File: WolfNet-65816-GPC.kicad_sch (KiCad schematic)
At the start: 1 part

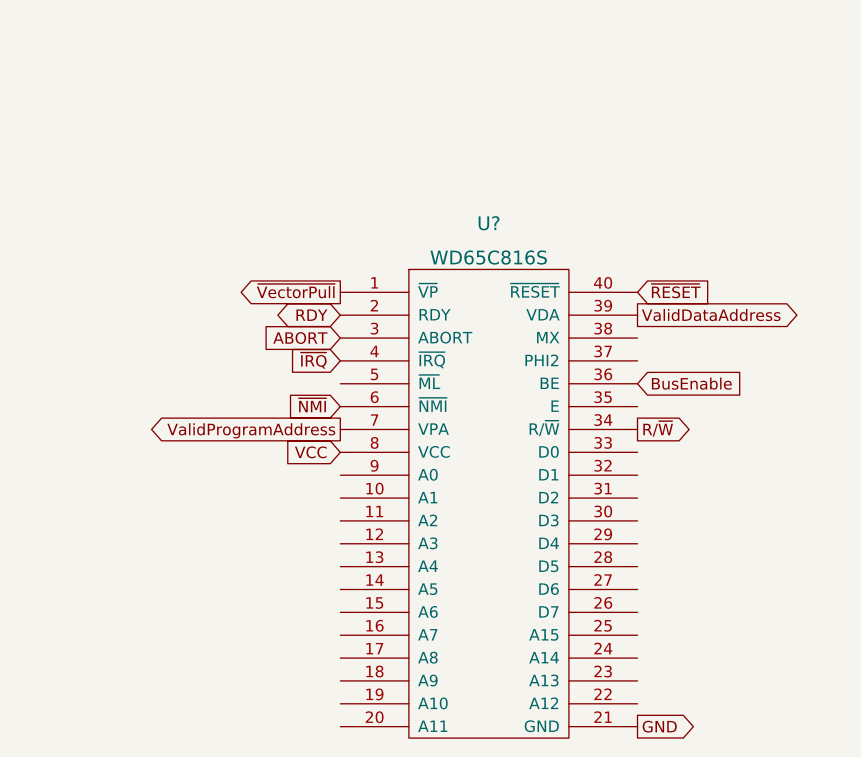
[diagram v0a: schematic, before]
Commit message: Added and connected CPU...
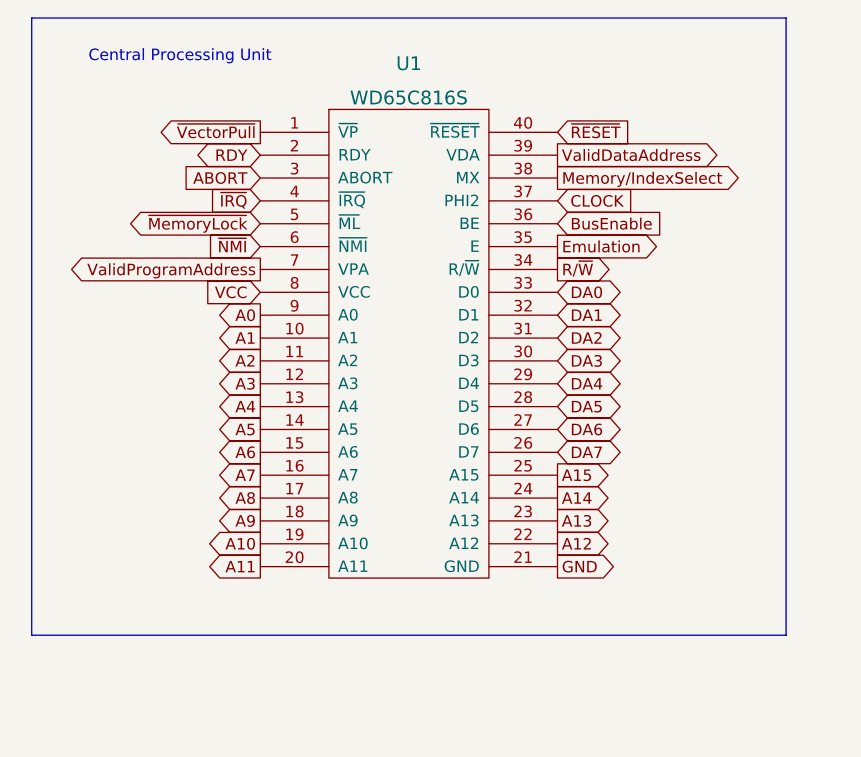
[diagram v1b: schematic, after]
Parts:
- gave numbers to parts that had none: 1
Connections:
- net A1: now reaches U1.10 (A1)
- net A2: now reaches U1.11 (A2)
- net A3: now reaches U1.12 (A3)
- net A4: now reaches U1.13 (A4)
- net A5: now reaches U1.14 (A5)
- net A6: now reaches U1.15 (A6)
- net A7: now reaches U1.16 (A7)
- net A8: now reaches U1.17 (A8)
- net A9: now reaches U1.18 (A9)
- net A10: now reaches U1.19 (A10)
- net A11: now reaches U1.20 (A11)
- net A12: now reaches U1.22 (A12)
- net A13: now reaches U1.23 (A13)
- net A14: now reaches U1.24 (A14)
- net A15: now reaches U1.25 (A15)
- net DA7: now reaches U1.26 (D7)
- net DA6: now reaches U1.27 (D6)
- net DA5: now reaches U1.28 (D5)
- net DA4: now reaches U1.29 (D4)
- net DA3: now reaches U1.30 (D3)
- net DA2: now reaches U1.31 (D2)
- net DA1: now reaches U1.32 (D1)
- net DA0: now reaches U1.33 (D0)
- net Emulation: now reaches U1.35 (E)
- net CLOCK: now reaches U1.37 (PHI2)
- net Memory/IndexSelect: now reaches U1.38 (MX)
- net ~{MemoryLock}: now reaches U1.5 (~{ML})
- net A0: now reaches U1.9 (A0)
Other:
- note added: "Central Processing Unit"
- moved on the sheet: U1

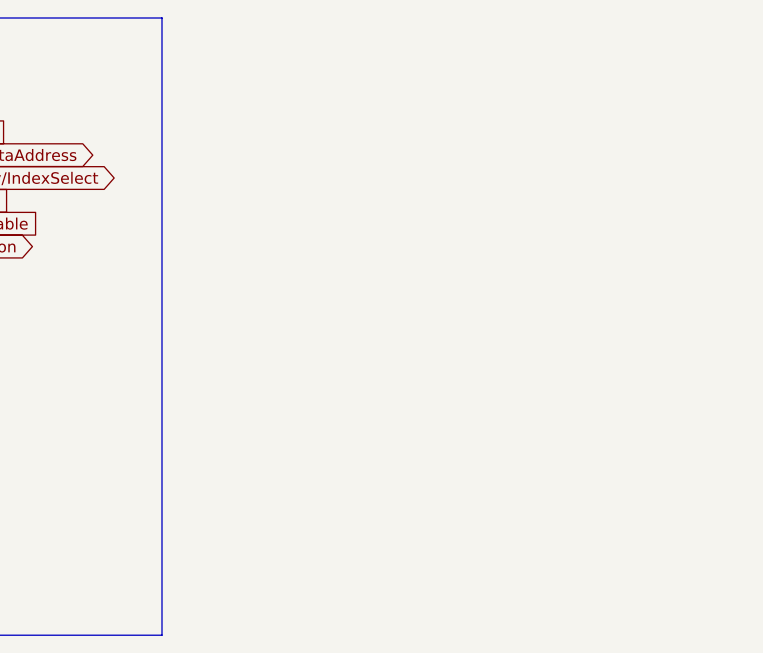
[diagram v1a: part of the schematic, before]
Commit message: Added and connected RAM...
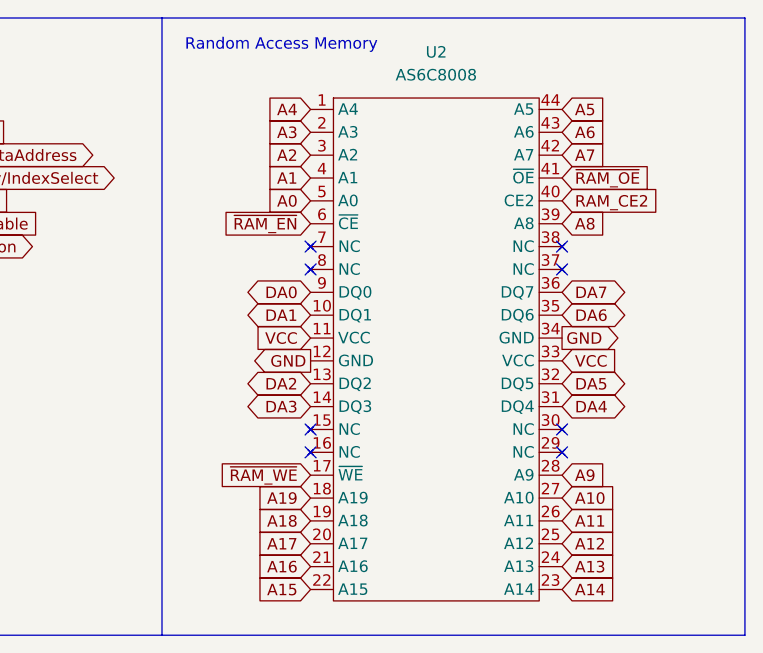
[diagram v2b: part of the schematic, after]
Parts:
- added U2: AS6C8008, symbol Memory:AS6C8008
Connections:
- net A0: now also U2.5 (A0)
- net A1: now also U2.4 (A1)
- net A10: now also U2.27 (A10)
- net A11: now also U2.26 (A11)
- net A12: now also U2.25 (A12)
- net A13: now also U2.24 (A13)
- net A14: now also U2.23 (A14)
- net A15: now also U2.22 (A15)
- net A2: now also U2.3 (A2)
- net A3: now also U2.2 (A3)
- net A4: now also U2.1 (A4)
- net A5: now also U2.44 (A5)
- net A6: now also U2.43 (A6)
- net A7: now also U2.42 (A7)
- net A8: now also U2.39 (A8)
- net A9: now also U2.28 (A9)
- net DA0: now also U2.9 (DQ0)
- net DA1: now also U2.10 (DQ1)
- net DA2: now also U2.13 (DQ2)
- net DA3: now also U2.14 (DQ3)
- net DA4: now also U2.31 (DQ4)
- net DA5: now also U2.32 (DQ5)
- net DA6: now also U2.35 (DQ6)
- net DA7: now also U2.36 (DQ7)
- net GND: now also U2.12 (GND), U2.34 (GND)
- net VCC: now also U2.11 (VCC), U2.33 (VCC)
- new net A16: U2.21 (A16)
- new net A17: U2.20 (A17)
- new net A18: U2.19 (A18)
- new net A19: U2.18 (A19)
- new net RAM_CE2: U2.40 (CE2)
- new net ~{RAM_EN}: U2.6 (~{CE})
- new net ~{RAM_OE}: U2.41 (~{OE})
- new net ~{RAM_WE}: U2.17 (~{WE})
- no-connect marks 0 -> 8
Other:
- note added: "Random Access Memory"

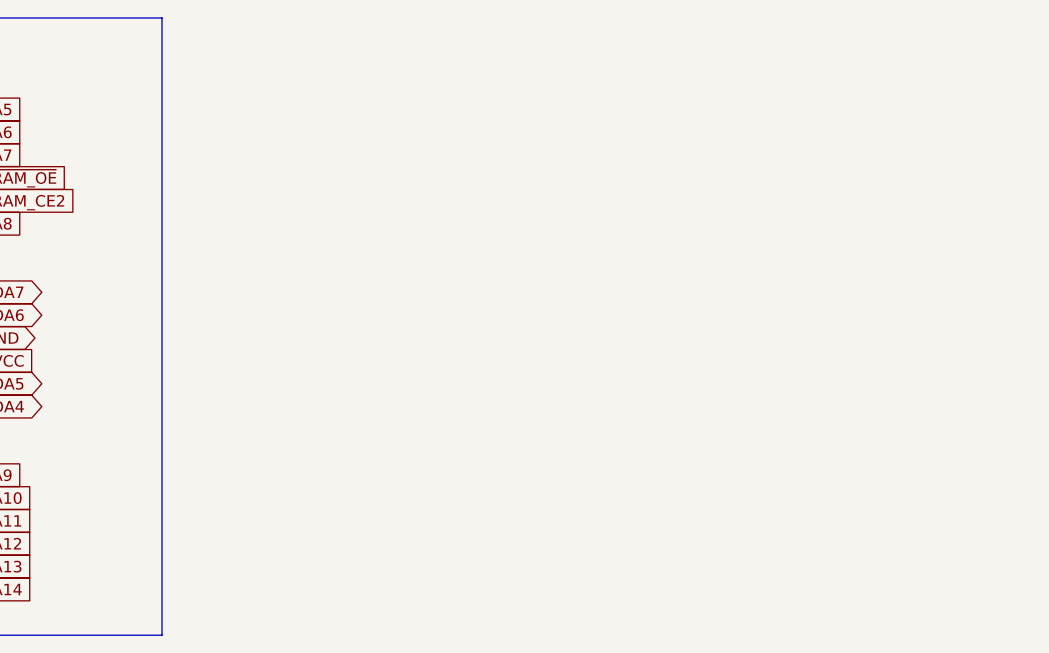
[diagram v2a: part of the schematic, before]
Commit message: Added and connected 2 ROM Banks...
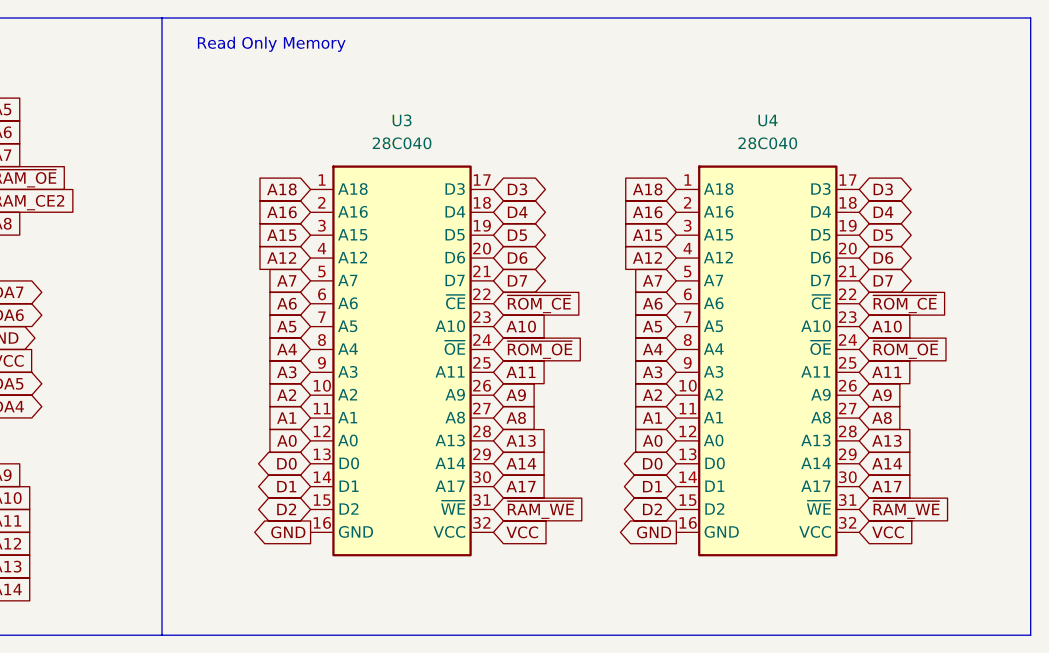
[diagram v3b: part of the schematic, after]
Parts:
- added U3, U4: 28C040, symbol Memory:28C040
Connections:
- net A0: now also U3.12 (A0), U4.12 (A0)
- net A1: now also U3.11 (A1), U4.11 (A1)
- net A10: now also U3.23 (A10), U4.23 (A10)
- net A11: now also U3.25 (A11), U4.25 (A11)
- net A12: now also U3.4 (A12), U4.4 (A12)
- net A13: now also U3.28 (A13), U4.28 (A13)
- net A14: now also U3.29 (A14), U4.29 (A14)
- net A15: now also U3.3 (A15), U4.3 (A15)
- net A16: now also U3.2 (A16), U4.2 (A16)
- net A17: now also U3.30 (A17), U4.30 (A17)
- net A18: now also U3.1 (A18), U4.1 (A18)
- net A2: now also U3.10 (A2), U4.10 (A2)
- net A3: now also U3.9 (A3), U4.9 (A3)
- net A4: now also U3.8 (A4), U4.8 (A4)
- net A5: now also U3.7 (A5), U4.7 (A5)
- net A6: now also U3.6 (A6), U4.6 (A6)
- net A7: now also U3.5 (A7), U4.5 (A7)
- net A8: now also U3.27 (A8), U4.27 (A8)
- net A9: now also U3.26 (A9), U4.26 (A9)
- net GND: now also U3.16 (GND), U4.16 (GND)
- net VCC: now also U3.32 (VCC), U4.32 (VCC)
- net ~{RAM_WE}: now also U3.31 (~{WE}), U4.31 (~{WE})
- new net D0: U3.13 (D0), U4.13 (D0)
- new net D1: U3.14 (D1), U4.14 (D1)
- new net D2: U3.15 (D2), U4.15 (D2)
- new net D3: U3.17 (D3), U4.17 (D3)
- new net D4: U3.18 (D4), U4.18 (D4)
- new net D5: U3.19 (D5), U4.19 (D5)
- new net D6: U3.20 (D6), U4.20 (D6)
- new net D7: U3.21 (D7), U4.21 (D7)
- new net ~{ROM_CE}: U3.22 (~{CE}), U4.22 (~{CE})
- new net ~{ROM_OE}: U3.24 (~{OE}), U4.24 (~{OE})
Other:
- note added: "Read Only Memory"

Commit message: Update WolfNet-65816-GPC.kicad_sch
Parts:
- removed U2: AS6C8008, symbol Memory:AS6C8008
- added SW1: SW_Push, symbol Switch:SW_Push
- added U5: 74HCT573, symbol 74xx:74LS573
- added U6: 74HCT245, symbol 74xx:74HC245
- added U7: 22V10, symbol GALs:22V10
- added U8: XCR3064XL-VQ100, Package_QFP:LQFP-100_14x14mm_P0.5mm, symbol CPLD_Xilinx:XCR3064XL-VQ100
- added U9: DS1813, symbol Supervisory Circuit:DS1813
- added U?: AS6C1608, symbol Memory:AS6C1608
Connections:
- net A0: now also U8.85 (A0), U?.5 (A0)
- net A1: now also U8.84 (A1), U?.4 (A1)
- net A10: now also U8.69 (A10), U?.27 (A10)
- net A11: now also U8.68 (A11), U?.26 (A11)
- net A12: now also U8.67 (A12), U?.25 (A12)
- net A13: now also U8.65 (A13), U?.24 (A13)
- net A14: now also U8.64 (A14), U?.23 (A14)
- net A15: now also U8.63 (A15), U?.22 (A15)
- net A16: now also U5.19 (Q0), U8.92 (B0), U?.21 (A16)
- net A17: now also U5.18 (Q1), U8.93 (B1), U?.20 (A17)
- net A18: now also U5.17 (Q2), U8.94 (B2), U?.19 (A18)
- net A19: now also U5.16 (Q3), U8.96 (B3), U?.18 (A19)
- net A2: now also U8.83 (A2), U?.3 (A2)
- net A3: now also U8.81 (A3), U?.2 (A3)
- net A4: now also U8.80 (A4), U?.1 (A4)
- net A5: now also U8.79 (A5), U?.44 (A5)
- net A6: now also U8.76 (A6), U?.43 (A6)
- net A7: now also U8.75 (A7), U?.42 (A7)
- net A8: now also U8.73 (A8/TDO), U?.39 (A8)
- net A9: now also U8.71 (A9), U?.28 (A9)
- net D0: now also U6.2 (A0), U?.9 (DQ0)
- net D1: now also U6.3 (A1), U?.10 (DQ1)
- net D2: now also U6.4 (A2), U?.13 (DQ2)
- net D3: now also U6.5 (A3), U?.14 (DQ3)
- net D4: now also U6.6 (A4), U?.31 (DQ4)
- net D5: now also U6.7 (A5), U?.32 (DQ5)
- net D6: now also U6.8 (A6), U?.35 (DQ6)
- net D7: now also U?.36 (DQ7)
- net DA0: now also U5.2 (D0), U6.18 (B0)
- net DA1: now also U5.3 (D1), U6.17 (B1)
- net DA2: now also U5.4 (D2), U6.16 (B2)
- net DA3: now also U5.5 (D3), U6.15 (B3)
- net DA4: now also U5.6 (D4), U6.14 (B4)
- net DA5: now also U5.7 (D5), U6.13 (B5)
- net DA6: now also U5.8 (D6), U6.12 (B6)
- net DA7: now also U5.9 (D7), U6.11 (B7)
- net GND: now also SW1.2, U5.1 (OE), U5.10 (GND), U6.10 (GND), U7.12 (GND), U8.26 (GND), U8.38 (GND), U8.43 (GND), U8.59 (GND), U8.74 (GND), U8.86 (GND), U8.95 (GND), U9.3 (GND), U?.12 (GND), U?.34 (GND)
- net RAM_CE2: now also U?.40 (CE2)
- net R/~{W}: now also U6.1 (A->B), U7.2 (IN)
- net ~{RAM_EN}: now also U?.6 (~{CE})
- net ~{RAM_OE}: now also U?.41 (~{OE})
- net ~{RAM_WE}: now also U?.17 (~{WE})
- net ~{RESET}: now also SW1.1, U9.1 (~{RST})
- net VCC renamed +5V
- net +5V: now also U5.20 (VCC), U6.20 (VCC), U7.24 (VCC), U8.18 (VCC), U8.3 (VCC), U8.34 (VCC), U8.39 (VCC), U8.51 (VCC), U8.66 (VCC), U8.82 (VCC), U8.91 (VCC), U9.2 (VCC), U?.11 (VCC), U?.33 (VCC)
- new net A20: U5.15 (Q4), U8.97 (B4), U?.16 (A20)
- new net A21: U5.14 (Q5), U8.98 (B5)
- new net A22: U5.13 (Q6), U8.99 (B6)
- new net A23: U5.12 (Q7), U8.100 (B7)
- new net D8: U6.9 (A7)
- new net DecoderJTAG: U8.11 (PORT_EN)
- new net NOT_PHI2: U5.11 (Load), U6.19 (CE), U7.23 (I/O)
- new net PHI2: U7.1 (CLK/IN), U8.90 (CLK0/IN0)
- new net READ: U7.22 (I/O)
- new net WRITE: U7.21 (I/O)
- no-connect marks 8 -> 7
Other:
- note added: "Address Decoding"
- note added: "Bank Address Latch"
- note added: "Direct Memory Access Circuit"
- note added: "Memory Management"
- note added: "Supervisory Circuit"

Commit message: Almost there...
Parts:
- added D?: PWR_OK1, symbol Device:LED
- added J1: ATX-24, symbol Connector:ATX-24
- added R?: 220 Ω, symbol Device:R
- added R?: PWR220T-20-5R00J, symbol Device:R
- added SW1: SW_SPST, symbol Switch:SW_SPST
- added U5: XCR3064XL-VQ100, Package_QFP:LQFP-100_14x14mm_P0.5mm, symbol CPLD_Xilinx:XCR3064XL-VQ100
- added U?: SC28L91, symbol UART:SC28L91
- added U?: MCP2200-I-SO, Package_SO:SOIC-20W_7.5x12.8mm_P1.27mm, symbol Interface_USB:MCP2200-I-SO
- gave numbers to parts that had none: 1
- renumbered SW1 to SW2, U9 to U10, U5 to U2, U6 to U3, U3 to U6, U4 to U7, U7 to U8, U8 to U9
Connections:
- net +5V: now also J1.21 (+5V), J1.22 (+5V), J1.23 (+5V), J1.4 (+5V), J1.6 (+5V), R?.1, U5.18 (VCC), U5.3 (VCC), U5.34 (VCC), U5.39 (VCC), U5.51 (VCC), U5.66 (VCC), U5.82 (VCC), U5.91 (VCC), U?.11 (VCC), U?.12 (MODE_SELECT), U?.44 (VCC)
- net A0: now also U?.2 (A0)
- net A1: now also U?.4 (A1)
- net A2: now also U?.6 (A2)
- net A3: now also U?.7 (A3)
- net GND: now also D?.1 (K), J1.15 (GND), J1.17 (GND), J1.18 (GND), J1.19 (GND), J1.24 (GND), J1.3 (GND), J1.5 (GND), J1.7 (GND), R?.2, SW1.1 (A), U5.26 (GND), U5.38 (GND), U5.43 (GND), U5.59 (GND), U5.74 (GND), U5.86 (GND), U5.95 (GND), U?.22 (GND)
- net PHI2: now also U5.90 (CLK0/IN0)
- net ~{RESET}: now also U?.4 (RST)
- net READ renamed ~{READ}
- net ~{READ}: now also U?.10 (~{RD})
- net WRITE renamed ~{WRITE}
- net ~{WRITE}: now also U?.9 (~{WR})
- new net: J1.8 (PWR_OK), R?.1
- new net: D?.2 (A), R?.2
- new net: J1.1 (+3.3V), J1.12 (+3.3V), J1.13 (+3.3V), J1.2 (+3.3V)
- new net: J1.16 (PS_ON#), SW1.2 (B)
- new net +12V: J1.10 (+12V), J1.11 (+12V)
- new net -12V: J1.14 (-12V)
- new net DMA_JTAG: U5.11 (PORT_EN)
- no-connect marks 7 -> 9
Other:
- note added: "ATX power connector"
- note added: "UART"
- note added: "USB Connection"

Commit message: Update WolfNet-65816-GPC.kicad_sch
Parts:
- removed U8: 22V10, symbol GALs:22V10
- added C?: 10 µF, symbol Device:C
- added D? (x2): GREEN, symbol Device:LED
- added J? (x4): Conn_01x01, symbol Connector_Generic:Conn_01x01
- added R? (x2): R, symbol Device:R
- added X?: ACO-12MHz, Oscillator:Oscillator_DIP-14, symbol Oscillator:ACO-xxxMHz
- added X?: ACO-xxxMHz, Oscillator:Oscillator_DIP-14, symbol Oscillator:ACO-xxxMHz
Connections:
- net +5V: now also X?.14 (Vcc), X?.14 (Vcc)
- net A8: now also J?.1 (Pin_1)
- net D0: now also U?.28 (D0)
- net D1: now also U?.18 (D1)
- net D2: now also U?.27 (D2)
- net D3: now also U?.19 (D3)
- net D4: now also U?.26 (D4)
- net D5: now also U?.20 (D5)
- net D6: now also U?.25 (D6)
- net D7: now also U?.21 (D7)
- net GND: now also U?.20 (VSS), C?.1, D?.1 (K), D?.1 (K), X?.7 (GND), X?.7 (GND)
- net NOT_PHI2: now also U9.4 (B8/TDI), J?.1 (Pin_1)
- net R/~{W}: now also U9.9 (B11); no longer U3.1 (A->B)
- net ~{IRQ}: now also U?.24 (~{IRQ})
- net ~{RAM_EN}: now also U9.37 (D15)
- net ~{READ}: now also U9.10 (B12)
- net ~{RESET}: now also U?.38 (RESET)
- net ~{WRITE}: now also U3.1 (A->B), U9.12 (B13)
- net at U9.15 (D0/TMS): now also J?.1 (Pin_1)
- net ~{UART_EN}: now reaches U9.29 (D8)
- net ~{UART_EN}: now also U?.39 (~{CE})
- net ~{ROM2_EN}: now reaches U9.31 (D10)
- net ~{ROM2_EN}: now also U7.22 (~{CE})
- net ~{ROM1_EN}: now reaches U9.33 (D12)
- net ~{ROM1_EN}: now also U6.22 (~{CE})
- net at U9.62 (C0/TCK): now also J?.1 (Pin_1)
- net TxD: now reaches U?.33 (TxD)
- net TxD: now also U?.12 (RX)
- net RxD: now reaches U?.35 (RxD)
- net RxD: now also U?.10 (TX)
- net at U?.36 (X1/CLK): now also X?.8 (OUT)
- net VBUS: now reaches U?.1 (VDD)
- net at U?.17 (V_USB): now also C?.2
- net USB_D-: now reaches U?.18 (D-)
- net USB_D+: now reaches U?.19 (D+)
- net at U?.2 (OSC1): now also X?.8 (OUT)
- net at U?.5 (GP7/TxLED): now also R?.1
- net at U?.6 (GP6/RxLED): now also R?.1
- net RAM_CE2 renamed RAM_EN2
- removed net ~{ROM_CE}: U6.22 (~{CE}), U7.22 (~{CE})
- net ~{ROM_OE} renamed ~{ROM1_OE}
- net ~{ROM1_OE}: no longer U7.24 (~{OE})
- new net: D?.2 (A), R?.2 (x2)
- new net ~{ROM2_OE}: U7.24 (~{OE})
- no-connect marks 9 -> 38
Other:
- note removed: "Memory Management"

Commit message: Update WolfNet-65816-GPC.kicad_sch
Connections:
- net RAM_EN2: now also U9.36 (D14)
- net ~{RAM_OE}: now also U9.35 (D13)
- net ~{ROM1_OE}: now also U9.32 (D11)
- net ~{ROM2_OE}: now also U9.30 (D9)
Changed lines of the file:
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@@
+    )
+  )
+  (global_label "RAM_EN2" (shape output) (at 336.55 109.22 0) (fields_autoplaced)
+    (effects (font (size 1.27 1.27)) (justify left))
+    (property "Intersheet References" "${INTERSHEET_REFS}" (id 0) (at 347.4298 109.1406 0)
+      (effects (font (size 1.27 1.27)) (justify left) hide)
     )
   )
@@
     )
   )
+  (global_label "~{ROM2_OE}" (shape output) (at 336.55 121.92 0) (fields_autoplaced)
+    (effects (font (size 1.27 1.27)) (justify left))
+    (property "Intersheet References" "${INTERSHEET_REFS}" (id 0) (at 347.6717 121.8406 0)
+      (effects (font (size 1.27 1.27)) (justify left) hide)
+    )
+  )
   (global_label "RxD" (shape output) (at 34.29 232.41 180) (fields_autoplaced)
     (effects (font (size 1.27 1.27)) (justify right))
@@
     )
   )
+  (global_label "~{RAM_OE}" (shape output) (at 336.55 111.76 0) (fields_autoplaced)
+    (effects (font (size 1.27 1.27)) (justify left))
+    (property "Intersheet References" "${INTERSHEET_REFS}" (id 0) (at 346.2202 111.6806 0)
+      (effects (font (size 1.27 1.27)) (justify left) hide)
+    )
+  )
   (global_label "A5" (shape input) (at 143.51 25.4 0) (fields_autoplaced)
     (effects (font (size 1.27 1.27)) (justify left))
@@
       (effects (font (size 1.27 1.27)) (justify left) hide)
     )
+  )
+  (global_label "~{ROM1_OE}" (shape output) (at 336.55 116.84 0) (fields_autoplaced)
+    (effects (font (size 1.27 1.27)) (justify left))
+    (property "Intersheet References" "${INTERSHEET_REFS}" (id 0) (at 347.6717 116.7606 0)
+      (effects (font (size 1.27 1.27)) (justify left) hide)
+    )

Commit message: Changing ROM to Flash memory...
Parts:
- added C? (x2): 0.33, symbol Device:C
- added C?: 10 µF, symbol Device:C_Polarized
- added J?: USB_B, symbol Connector:USB_B
- added JP?: Jumper_3_Bridged12, symbol Jumper:Jumper_3_Bridged12
- added R? (x3): 3.3k, symbol Device:R
- added U?: SST39SF040, symbol Memory_Flash:SST39SF040
- added U?: LM7905_TO220, Package_TO_SOT_THT:TO-220-3_Vertical, symbol Regulator_Linear:LM7905_TO220
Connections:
- net +12V: now also C?.1, U?.2 (VI)
- net +5V: now also R?.1, R?.1, R?.1
- net A0: now also U?.12 (A0)
- net A1: now also U?.11 (A1)
- net A2: now also U?.10 (A2)
- net A3: now also U?.9 (A3)
- net D0: now also U?.13 (D0)
- net D1: now also U?.14 (D1)
- net D2: now also U?.15 (D2)
- net D3: now also U?.17 (D3)
- net D4: now also U?.18 (D4)
- net D5: now also U?.19 (D5)
- net D6: now also U?.20 (D6)
- net D7: now also U?.21 (D7)
- net Emulation: now also U9.9 (B11)
- net GND: now also C?.2, C?.2, C?.2, J?.4 (GND), J?.5 (Shield), U?.1 (GND), U?.16 (GND)
- net RDY: now also R?.2
- net R/~{W}: now also U9.10 (B12), U?.31 (PGM); no longer U9.9 (B11)
- net USB_D+: now also J?.3 (D+)
- net USB_D-: now also J?.2 (D-)
- net VBUS: now also C?.1, J?.1 (VBUS)
- net ValidDataAddress: now also U9.8 (B10)
- net ValidProgramAddress: now also U9.6 (B9)
- net ~{IRQ}: now also JP?.1 (A), R?.2; no longer U?.24 (~{IRQ})
- net ~{NMI}: now also JP?.3 (B), R?.2
- net ~{READ}: now also U9.12 (B13); no longer U9.10 (B12)
- net ~{WRITE}: now also U9.13 (B14); no longer U9.12 (B13)
- net ~{RAM_WE} renamed ~{RW}
- new net: JP?.2 (C), U?.24 (~{IRQ})
- new net -5V: C?.1, U?.3 (VO)
- new net VCC: U?.32 (VCC)
- new net ~{FLASH_EN}: U?.22 (CE)
- new net ~{FLASH_OE}: U?.24 (OE)
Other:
- note added: "-5v Regulator"
- note added: "USB Connector"
